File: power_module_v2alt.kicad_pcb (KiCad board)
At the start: 4 copper layers, 100 x 85 mm, 77 parts, among them J1_BMS1 I2C+ALERT, J1_INPUT1 USB_C_16P, Q1_BMS1 AON7544, Q1_BUCKBOOST1 AON7544, Q2_BMS1 AON7544, Q2_BUCKBOOST1 AON7544, Q3_BUCKBOOST1 AON7544, Q4_BUCKBOOST1 AON7544, SW1_BMS1 Kill Switch, U1_BMS1 BQ7692003PWR, U1_BUCKBOOST1 LM5176PWP, U1_CHARGER1 IP2326, U1_INPUT1 CH224K

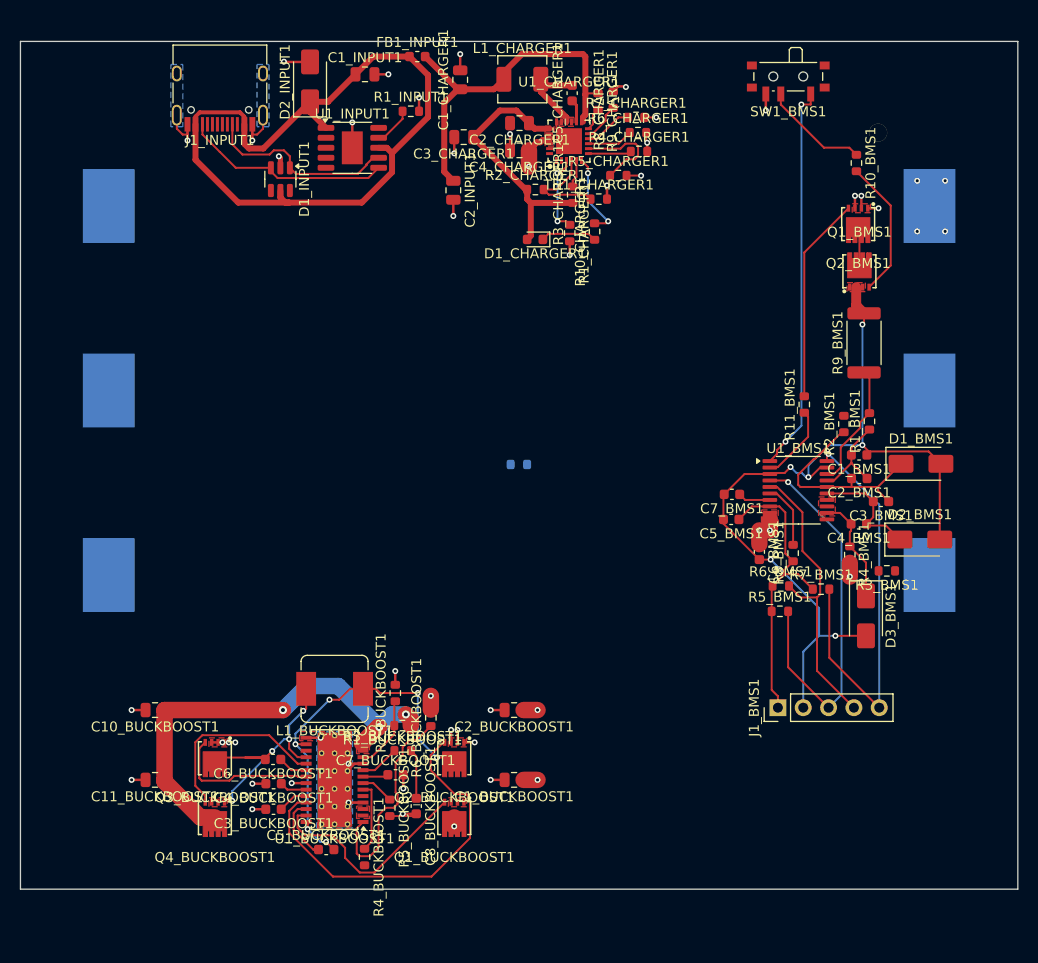
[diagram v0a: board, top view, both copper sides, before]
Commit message: Step 7 iterate: scrub buckboost + relax passives + reroute + via finisher
Bulk caps C1/C2/C10/C11 were floating at buckboost periphery because
both pin nets were PLANE-classified (BAT+/GND/VOUT_12V all PLANE via
META1) — placer had zero attraction to LM5176.  Fresh cycle to reset:

Pipeline
1. scrub_region on all 22 buckboost refs (margin 2mm) — deleted 166
   tracks + 36 vias + 8 pin-zones on 20 nets.  Cross-region traces
   spared (endpoint-outside-hull rule), plane pours untouched (F.Cu
   +B.Cu only).
2. relax_placement with Q1-Q4 + L1 + U1 LOCKED, only the 16
   passives moving.  Buck-boost topology preserved; bulk caps pulled
   in to their DECOUPLING targets (LM5176.2/3 for input, .12/.13
   for output).  Small comp-loop caps parked around LM5176 body.
3. pin_zone_same_net on the moved buckboost components — 13 zones
   re-applied for LM5176 EP fanout + Q source pads.
4. Full autoroute — 413 tracks + 47 vias (net-added +8 tracks
   +24 vias vs pre-scrub baseline at 405+23).  autoDedupe of 180
   duplicates from ImportSpecctraSES append behaviour is expected.
5. via_orphan_pads GND (+22) / BAT+ (+3) / VOUT_12V (+5) — the
   last two nets are now needed because VOUT_12V bulks became
   plane-attached rather than trace-routed.
6. refill_zones + DRC.

Result: 24 unconnected → 24 (was 26 before scrub).  Mostly the same
holdouts: BAT1 cell-sense cross-layer wires (CELL1/2_TOP, BAT-, one
BAT+), signal-level stragglers freerouting can't reach (SW1×4,
SW2×2, HDRV1, LDRV1/2, FB, VSS, TS1), and 4 GND pin-zone → plane
gaps.  Buckboost signal stragglers can be knocked out with
route_pad_to_pad + find_via_lane in the finisher pass.

Co-Authored-By: Claude Opus 4.7 <noreply@anthropic.com>
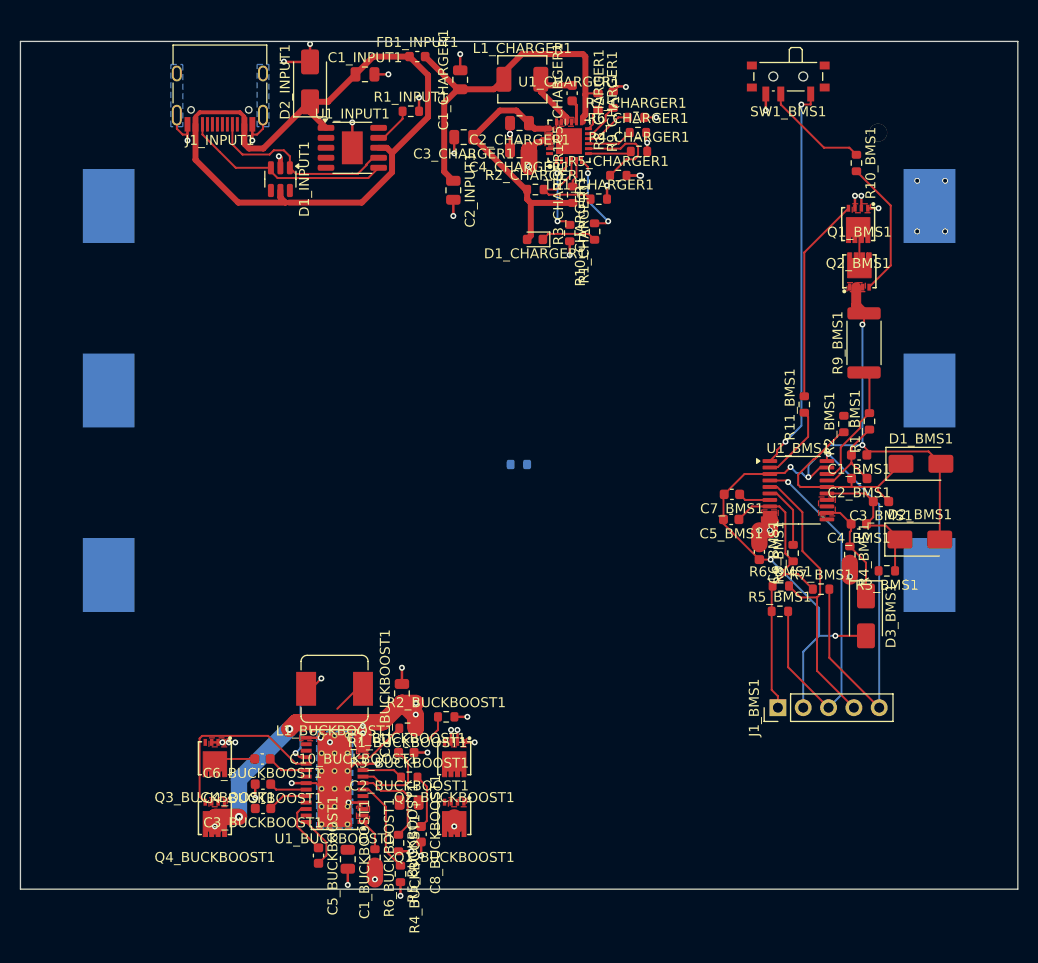
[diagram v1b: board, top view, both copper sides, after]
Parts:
- moved C11_BUCKBOOST1 26.2 mm to (38.2, 65.4), turned to 90 degrees
- moved C10_BUCKBOOST1 20.1 mm to (33.4, 70.3)
- moved C1_BUCKBOOST1 18.5 mm to (32.8, 82.0), turned to -90 degrees
- moved R6_BUCKBOOST1 15.1 mm to (35.5, 81.8), turned to -90 degrees
- moved C2_BUCKBOOST1 14.0 mm to (39.0, 76.3), turned to 0 degrees
- moved R2_BUCKBOOST1 5.64 mm to (42.7, 67.7), turned to 0 degrees
- moved R4_BUCKBOOST1 3.98 mm to (38.1, 83.5)
- moved R5_BUCKBOOST1 3.64 mm to (37.9, 80.4)
- moved C8_BUCKBOOST1 2.87 mm to (40.2, 79.5)
- moved R3_BUCKBOOST1 2.75 mm to (39.0, 73.8)
- moved C7_BUCKBOOST1 2.47 mm to (38.7, 71.3)
- moved C4_BUCKBOOST1 1.07 mm to (24.3, 74.5)
- moved C6_BUCKBOOST1 1.06 mm to (24.3, 71.9)
- moved C3_BUCKBOOST1 1.05 mm to (24.3, 76.9)
- moved C5_BUCKBOOST1 0.98 mm to (29.9, 81.6), turned to -90 degrees
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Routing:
- net LDRV1: track 38.3 -> 0.00 mm
- net SW1: track 38.7 -> 8.72 mm, vias 6 -> 0
- net HDRV1: track 22.2 -> 0.00 mm
- net BB_EN: track 21.5 -> 3.22 mm
- net LDRV2: track 14.9 -> 0.00 mm
- net SW2: track 26.7 -> 15.8 mm, vias 4 -> 2
- net VOUT_12V: track 44.8 -> 36.8 mm, vias 3 -> 7
- net SLOPE: track 3.37 -> 9.32 mm
- net GND: track 75.1 -> 81.0 mm, vias 40 -> 43
- net SS: track 2.57 -> 8.37 mm
- net VC2: track 11.6 -> 14.9 mm
- net RT: track 7.07 -> 9.52 mm
- net BAT+: track 13.1 -> 11.9 mm, vias 12 -> 11
- net BOOT2: track 2.99 -> 4.07 mm
- net LM5176_VCC: track 2.74 -> 3.78 mm
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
